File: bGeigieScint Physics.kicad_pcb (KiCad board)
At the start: 2 copper layers, 6 parts, among them U1 TMP116xxDRV, U2 AT24CS01-STUM

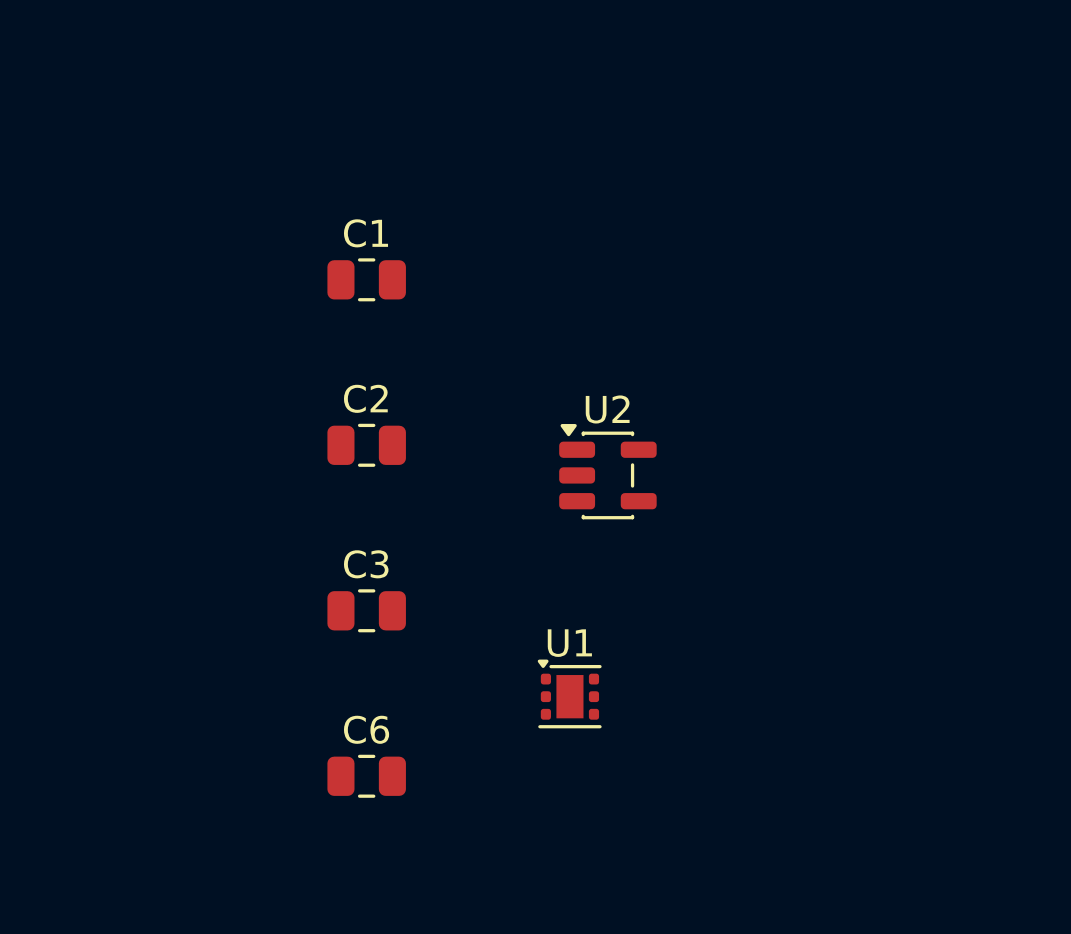
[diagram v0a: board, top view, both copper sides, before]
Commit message: Add AFBRS4N44P014M component to KiCad libraries
- Created new module file for AFBRS4N44P014M in Kicad libs with detailed footprint and pad definitions.
- Added corresponding module entry in the bGeigieScint.pretty library.
- Updated fp-lib-table to include new library paths for proper integration.
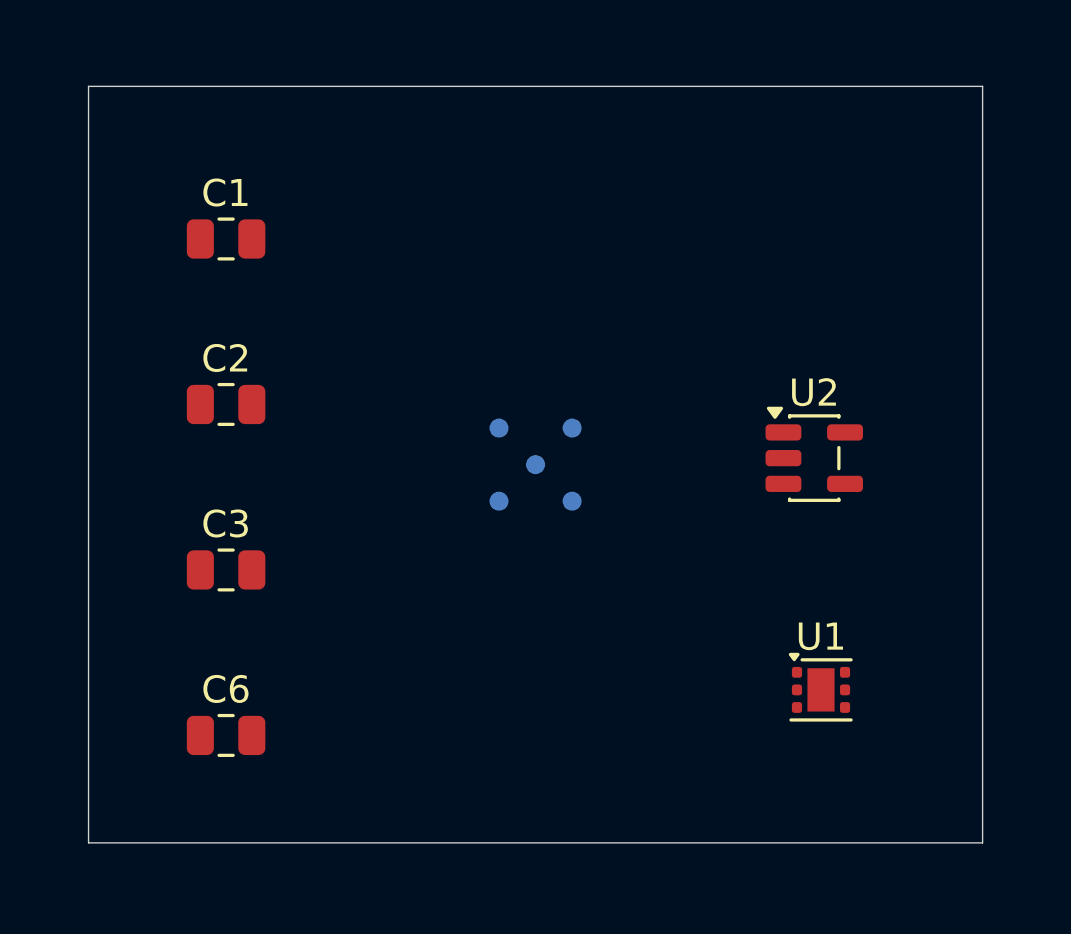
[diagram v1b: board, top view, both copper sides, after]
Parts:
- added U3: AFBR-S4N44P014M, bGeigieScint:AFBRS4N44P014M, B.Cu at (146.1, 92.6)
- moved U1 9.28 mm to (156.6, 101.0)
- moved U2 7.65 mm to (156.3, 92.4)
- moved C2 5.41 mm to (134.6, 90.4)
- moved C3 5.41 mm to (134.6, 96.5)
- moved C1 5.41 mm to (134.6, 84.3)
- moved C6 5.41 mm to (134.6, 102.6)
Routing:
- added copper zone on In1.Cu, net /GND
- added copper zone on In2.Cu, net /GND
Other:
- board outline added: 33 x 27.9 mm
- copper layers 2 -> 4

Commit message: Add bootloader update for Pomelo C37721D with new firmware
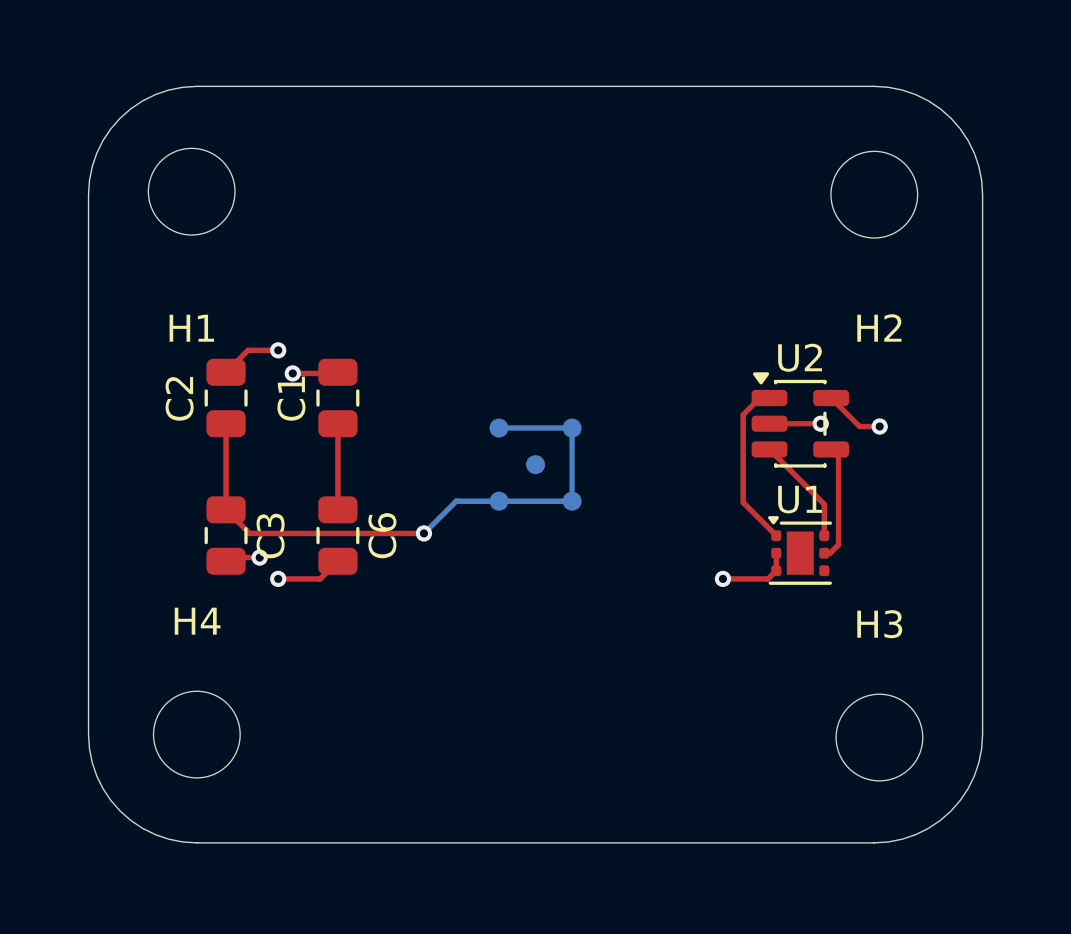
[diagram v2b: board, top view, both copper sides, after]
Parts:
- added H1: MountingHole_3.2mm_M3, MountingHole:MountingHole_3.2mm_M3, F.Cu at (133.3, 82.5)
- added H2: MountingHole_3.2mm_M3, MountingHole:MountingHole_3.2mm_M3, F.Cu at (158.6, 82.7)
- added H3: MountingHole_3.2mm_M3, MountingHole:MountingHole_3.2mm_M3, F.Cu at (158.8, 102.7)
- added H4: MountingHole_3.2mm_M3, MountingHole:MountingHole_3.2mm_M3, F.Cu at (133.5, 102.6)
- moved C6 8.46 mm to (138.8, 95.2), turned to -90 degrees
- moved C1 7.18 mm to (138.8, 90.2), turned to 90 degrees
- moved U1 5.11 mm to (155.8, 95.9)
- moved U2 1.37 mm to (155.8, 91.1)
- moved C3 1.27 mm to (134.6, 95.2), turned to -90 degrees
- moved C2 0.24 mm to (134.6, 90.2), turned to 90 degrees
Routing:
- net /SiPM_K: track 0.00 -> 22.2 mm, vias 0 -> 1
- net /GND: track 0.00 -> 14.6 mm, vias 0 -> 7
- net /PA17: track 0.00 -> 6.20 mm
- net /3V3: track 0.00 -> 4.29 mm
- net /PA16: track 0.00 -> 4.02 mm
- net Net-(C1-Pad1): track 0.00 -> 3.18 mm
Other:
- outline, holes or cut-outs redrawn

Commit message: Add UART test script for PomeloCore
This commit introduces a new Python script, test_uart.py, designed to test UART communication with the PomeloCore. The script opens a specified serial port, sends a series of commands, and displays the responses. It handles potential exceptions and allows for testing on multiple ports.
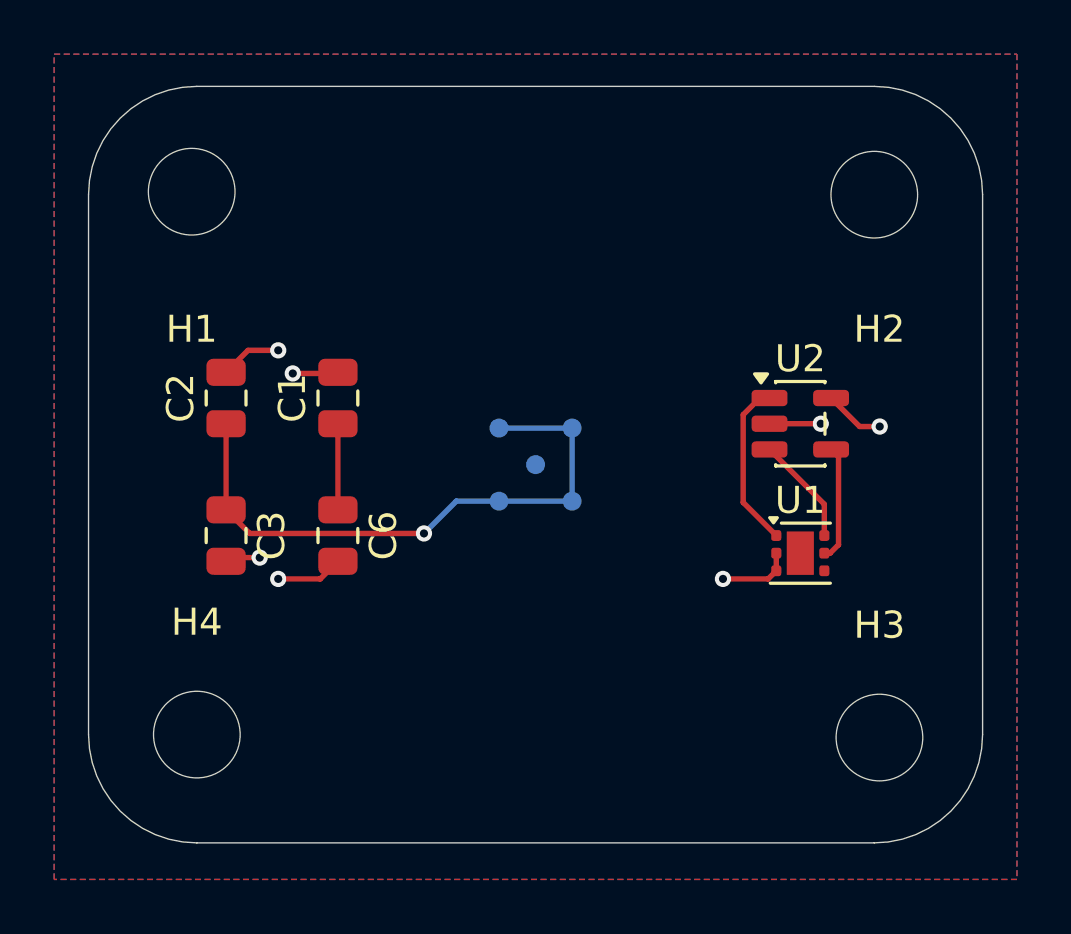
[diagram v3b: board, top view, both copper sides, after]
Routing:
- added copper zone on B.Cu, net /GND
- added copper zone on F.Cu, net /GND
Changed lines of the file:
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@@
+		(net 1)
+		(net_name "/GND")
+		(layers "F.Cu" "B.Cu" "In1.Cu" "In2.Cu")
+		(hatch edge 0.5)
+		(priority 2)
+		(connect_pads
+			(clearance 0.5)
+		)
+		(min_thickness 0.25)
+		(filled_areas_thickness no)
+		(fill yes
+			(thermal_gap 0.5)
+			(thermal_bridge_width 0.5)
+		)
+		(polygon
+			(pts
+				(xy 128.27 77.47) (xy 163.83 77.47) (xy 163.83 107.95) (xy 128.27 107.95)
+			)
+		)
+	)
+	(zone
 		(net 1)
 		(net_name "/GND")
